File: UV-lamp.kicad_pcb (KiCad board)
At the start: 2 copper layers, 32 parts, among them IC1 ATMEGA8-P, P1 CONN_2, P2 CONN_2, Q1 MOSFET_N, Q2 NPN, Q3 NPN, Q4 NPN, SW1 SW_PUSH, SW2 SW_PUSH, SW3 SW_PUSH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

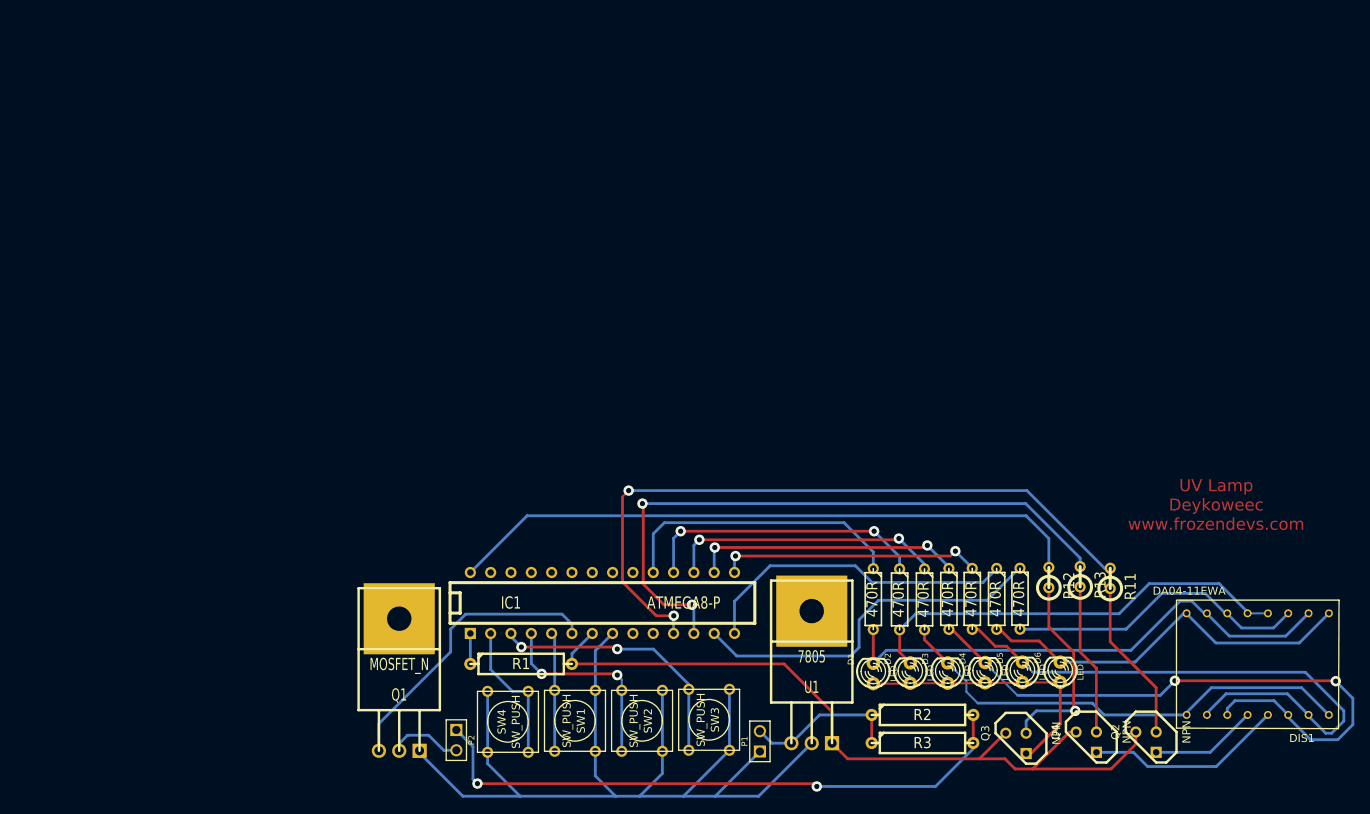
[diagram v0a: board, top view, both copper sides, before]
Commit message: Add license notice to the schematic and PCB layout
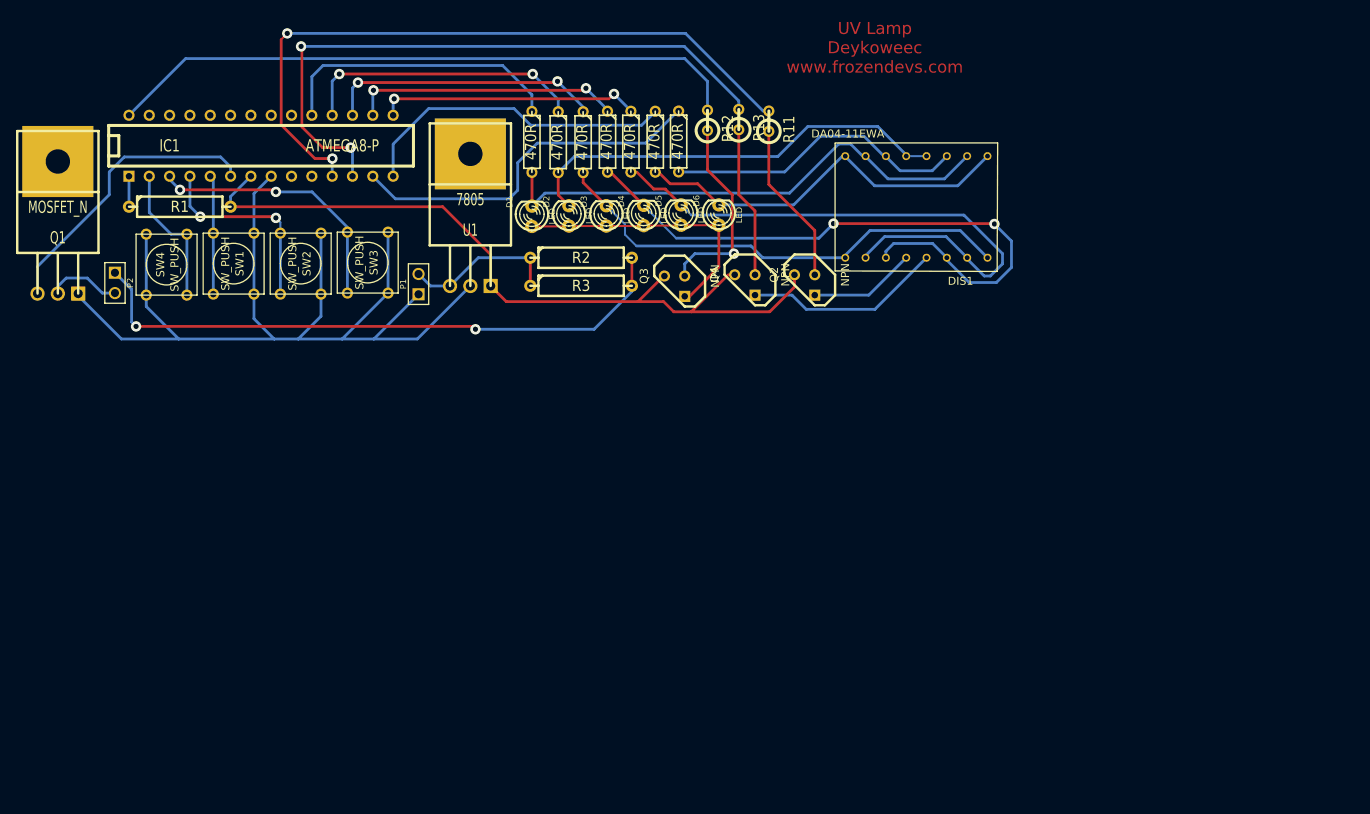
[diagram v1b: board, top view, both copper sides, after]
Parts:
- moved R12 71.3 mm to (172.3, 91.9)
- moved R2 71.3 mm to (156.5, 109.1)
- moved P2 71.3 mm to (98.2, 112.3)
- moved D1 71.3 mm to (150.3, 103.9)
- moved D2 71.3 mm to (154.9, 103.9)
- moved D3 71.3 mm to (159.6, 103.9)
- moved D4 71.3 mm to (164.3, 103.8)
- moved D5 71.3 mm to (169.0, 103.8)
- moved D6 71.3 mm to (173.7, 103.8)
- moved DIS1 71.3 mm to (198.4, 102.8)
- moved IC1 71.3 mm to (116.5, 95.1)
- moved P1 71.3 mm to (136.1, 112.4)
- moved Q1 71.3 mm to (91.1, 113.6)
- moved Q2 71.3 mm to (184.4, 112.5)
- moved Q3 71.3 mm to (168.1, 112.7)
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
